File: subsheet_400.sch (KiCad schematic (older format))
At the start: 24 parts, among them U400 STE_GSTMCU_PHY

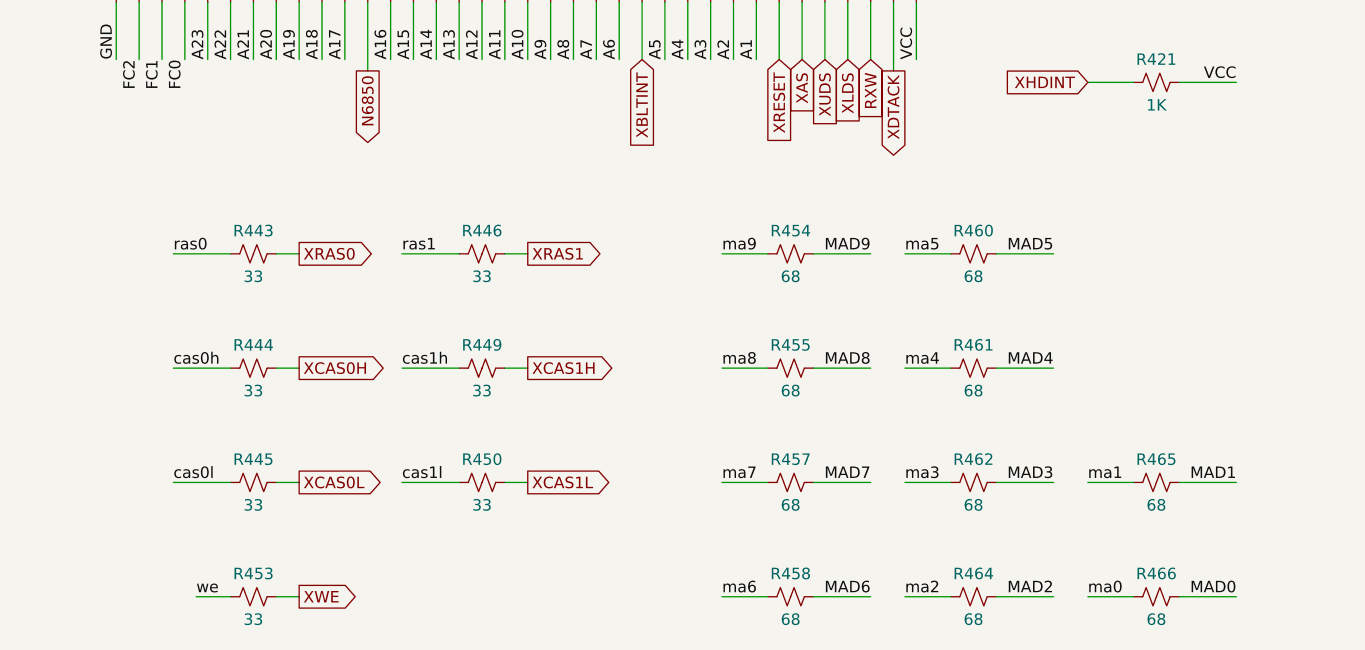
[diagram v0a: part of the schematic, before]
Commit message: Resolves #1 : Use 4-resistor packs wherever it is possible
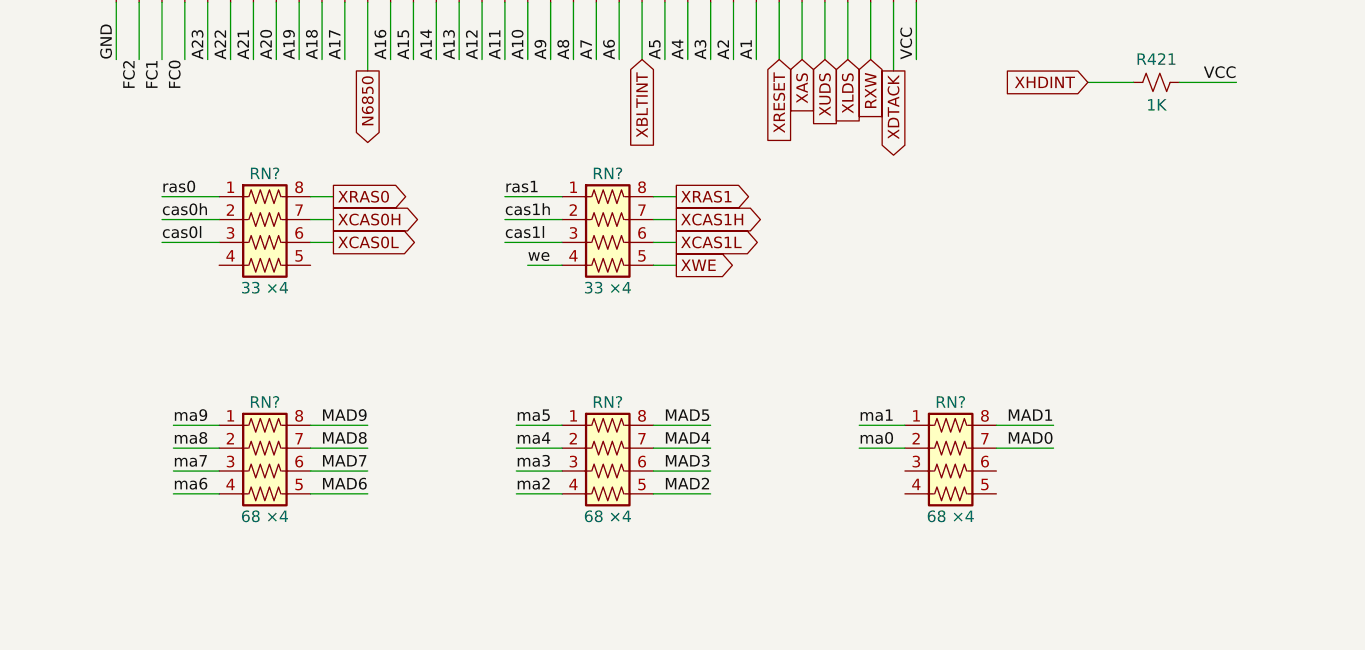
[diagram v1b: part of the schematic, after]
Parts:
- removed R443, R444, R445, R446, R449, R450, R453: 33, commons_passives_THT:Passive_THT_resistor_W2.54mm_L12.70mm, symbol Device:R_Small_US
- removed R454, R455, R457, R458, R460, R461, R462, R464, R465, R466: 68, commons_passives_THT:Passive_THT_resistor_W2.54mm_L12.70mm, symbol Device:R_Small_US
- added RN? (x2): 33 ×4, symbol custom_passives:R_Pack04_US
- added RN? (x3): 68 ×4, symbol custom_passives:R_Pack04_US
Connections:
- net MAD0: now also RN?.7 (R2.2)
- net MAD1: now also RN?.8 (R1.2)
- net MAD2: now also RN?.5 (R4.2)
- net MAD3: now also RN?.6 (R3.2)
- net MAD4: now also RN?.7 (R2.2)
- net MAD5: now also RN?.8 (R1.2)
- net MAD6: now also RN?.5 (R4.2)
- net MAD7: now also RN?.6 (R3.2)
- net MAD8: now also RN?.7 (R2.2)
- net MAD9: now also RN?.8 (R1.2)
- net XCAS0H: now also RN?.7 (R2.2)
- net XCAS0L: now also RN?.6 (R3.2)
- net XCAS1H: now also RN?.7 (R2.2)
- net XCAS1L: now also RN?.6 (R3.2)
- net XRAS0: now also RN?.8 (R1.2)
- net XRAS1: now also RN?.8 (R1.2)
- net XWE: now also RN?.5 (R4.2)
- net cas0h: now also RN?.2 (R2.1)
- net cas0l: now also RN?.3 (R3.1)
- net cas1h: now also RN?.2 (R2.1)
- net cas1l: now also RN?.3 (R3.1)
- net ma0: now also RN?.2 (R2.1)
- net ma1: now also RN?.1 (R1.1)
- net ma2: now also RN?.4 (R4.1)
- net ma3: now also RN?.3 (R3.1)
- net ma4: now also RN?.2 (R2.1)
- net ma5: now also RN?.1 (R1.1)
- net ma6: now also RN?.4 (R4.1)
- net ma7: now also RN?.3 (R3.1)
- net ma8: now also RN?.2 (R2.1)
- net ma9: now also RN?.1 (R1.1)
- net ras0: now also RN?.1 (R1.1)
- net ras1: now also RN?.1 (R1.1)
- net we: now also RN?.4 (R4.1)

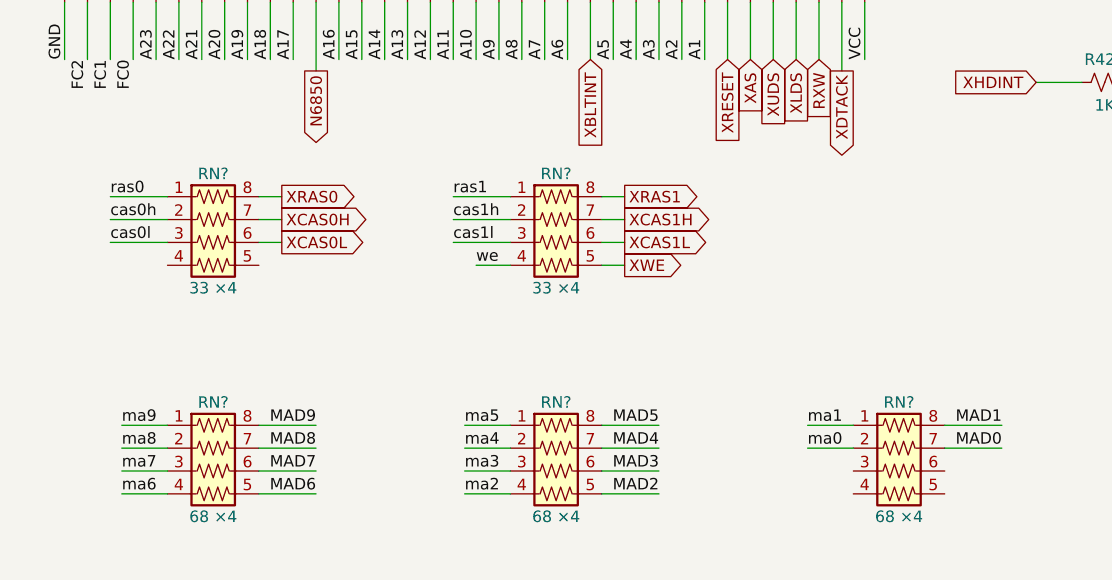
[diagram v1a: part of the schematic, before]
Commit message: annotate resistor networks and mark unused pins as unconnected
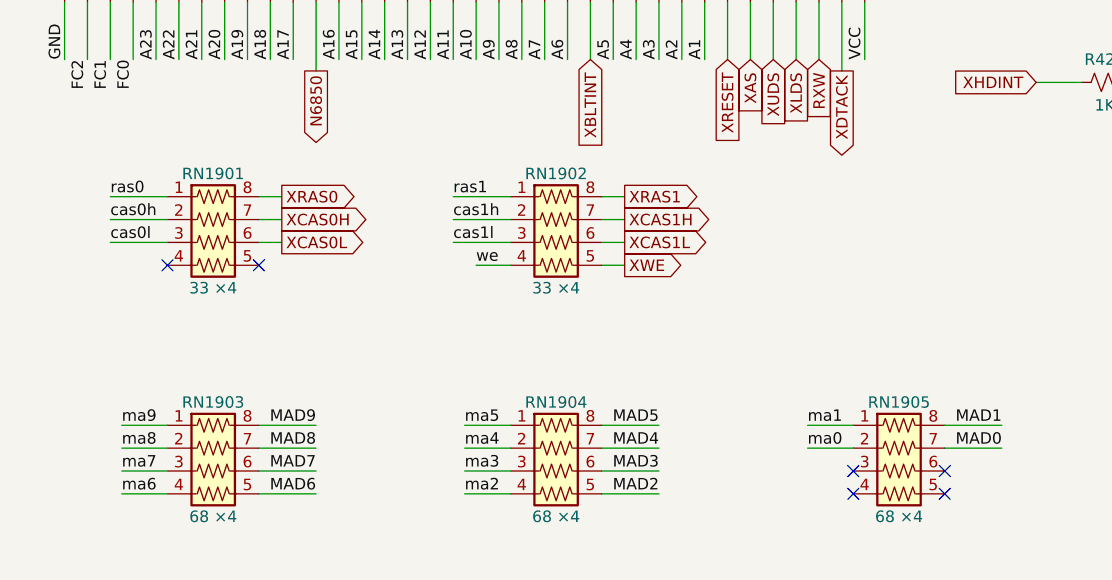
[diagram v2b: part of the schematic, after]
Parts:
- gave numbers to parts that had none: 5
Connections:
- no-connect marks 12 -> 18
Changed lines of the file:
@@
 	3550 7400 3550 7150
 $Comp
-L custom_passives:R_Pack04_US RN?
+L custom_passives:R_Pack04_US RN1901
 U 1 1 6229461F
 P 3000 8200
-F 0 "RN?" V 2700 8200 50  0000 C CNN
+F 0 "RN1901" V 2700 8200 50  0000 C CNN
 F 1 "33 ×4" V 3200 8200 50  0000 C CNN
 F 2 "" V 3275 8200 50  0001 C CNN
@@
 $EndComp
 $Comp
-L custom_passives:R_Pack04_US RN?
+L custom_passives:R_Pack04_US RN1902
 U 1 1 622CCFB9
 P 4500 8200
-F 0 "RN?" V 4200 8200 50  0000 C CNN
+F 0 "RN1902" V 4200 8200 50  0000 C CNN
 F 1 "33 ×4" V 4700 8200 50  0000 C CNN
 F 2 "" V 4775 8200 50  0001 C CNN
@@
 $EndComp
 $Comp
-L custom_passives:R_Pack04_US RN?
+L custom_passives:R_Pack04_US RN1903
 U 1 1 6233CA32
 P 3000 9200
-F 0 "RN?" V 2700 9200 50  0000 C CNN
+F 0 "RN1903" V 2700 9200 50  0000 C CNN
 F 1 "68 ×4" V 3200 9200 50  0000 C CNN
 F 2 "" V 3275 9200 50  0001 C CNN
@@
 $EndComp
 $Comp
-L custom_passives:R_Pack04_US RN?
+L custom_passives:R_Pack04_US RN1904
 U 1 1 623874D8
 P 4500 9200
-F 0 "RN?" V 4200 9200 50  0000 C CNN
+F 0 "RN1904" V 4200 9200 50  0000 C CNN
 F 1 "68 ×4" V 4700 9200 50  0000 C CNN
 F 2 "" V 4775 9200 50  0001 C CNN
@@
 $EndComp
 $Comp
-L custom_passives:R_Pack04_US RN?
+L custom_passives:R_Pack04_US RN1905
 U 1 1 623D2AD5
 P 6000 9200
-F 0 "RN?" V 5700 9200 50  0000 C CNN
+F 0 "RN1905" V 5700 9200 50  0000 C CNN
 F 1 "68 ×4" V 6200 9200 50  0000 C CNN
 F 2 "" V 6275 9200 50  0001 C CNN
@@
 	0    1    1    0
 $EndComp
+NoConn ~ 2800 8300
+NoConn ~ 3200 8300
+NoConn ~ 5800 9200
+NoConn ~ 6200 9200
+NoConn ~ 5800 9300
+NoConn ~ 6200 9300
 $EndSCHEMATC

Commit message: Resolves #7 : Assign SMD footprints to resistors pack
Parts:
- RN1901, RN1902, RN1903, RN1904, RN1905: footprint (none) -> Resistor_SMD:R_Array_Convex_4x0603
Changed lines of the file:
@@
 F 0 "RN1901" V 2700 8200 50  0000 C CNN
 F 1 "33 ×4" V 3200 8200 50  0000 C CNN
-F 2 "" V 3275 8200 50  0001 C CNN
+F 2 "Resistor_SMD:R_Array_Convex_4x0603" V 3275 8200 50  0001 C CNN
 F 3 "~" H 3000 8200 50  0001 C CNN
 	1    3000 8200
@@
 F 0 "RN1902" V 4200 8200 50  0000 C CNN
 F 1 "33 ×4" V 4700 8200 50  0000 C CNN
-F 2 "" V 4775 8200 50  0001 C CNN
+F 2 "Resistor_SMD:R_Array_Convex_4x0603" V 4775 8200 50  0001 C CNN
 F 3 "~" H 4500 8200 50  0001 C CNN
 	1    4500 8200
@@
 F 0 "RN1903" V 2700 9200 50  0000 C CNN
 F 1 "68 ×4" V 3200 9200 50  0000 C CNN
-F 2 "" V 3275 9200 50  0001 C CNN
+F 2 "Resistor_SMD:R_Array_Convex_4x0603" V 3275 9200 50  0001 C CNN
 F 3 "~" H 3000 9200 50  0001 C CNN
 	1    3000 9200
@@
 F 0 "RN1904" V 4200 9200 50  0000 C CNN
 F 1 "68 ×4" V 4700 9200 50  0000 C CNN
-F 2 "" V 4775 9200 50  0001 C CNN
+F 2 "Resistor_SMD:R_Array_Convex_4x0603" V 4775 9200 50  0001 C CNN
 F 3 "~" H 4500 9200 50  0001 C CNN
 	1    4500 9200
@@
 F 0 "RN1905" V 5700 9200 50  0000 C CNN
 F 1 "68 ×4" V 6200 9200 50  0000 C CNN
-F 2 "" V 6275 9200 50  0001 C CNN
+F 2 "Resistor_SMD:R_Array_Convex_4x0603" V 6275 9200 50  0001 C CNN
 F 3 "~" H 6000 9200 50  0001 C CNN
 	1    6000 9200

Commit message: Resolves #13 : assign 1206 hand-solder footprints to resistors
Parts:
- R421: footprint commons_passives_THT:Passive_THT_resistor_W2.54mm_L12.70mm -> Resistor_SMD:R_1206_3216Metric_Pad1.30x1.75mm_HandSolder
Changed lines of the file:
@@
 F 0 "R421" V 6800 7500 50  0000 C CNN
 F 1 "1K" V 7000 7500 50  0000 C CNN
-F 2 "commons_passives_THT:Passive_THT_resistor_W2.54mm_L12.70mm" H 6900 7500 50  0001 C CNN
+F 2 "Resistor_SMD:R_1206_3216Metric_Pad1.30x1.75mm_HandSolder" H 6900 7500 50  0001 C CNN
 F 3 "~" H 6900 7500 50  0001 C CNN
 	1    6900 7500

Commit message: Resolves #8 : Assign 1206 hand-solder footprints to non polarized capacitors
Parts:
- C402, C403, C404, C405, C406: footprint commons_passives_THT:Passive_THT_capacitor_mlcc_W2.54mm_L7.62mm -> Capacitor_SMD:C_1206_3216Metric_Pad1.33x1.80mm_HandSolder
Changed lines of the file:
@@
 F 0 "C402" H 1125 7350 50  0000 L CNN
 F 1 "0.1uF" H 1125 7150 50  0000 L CNN
-F 2 "commons_passives_THT:Passive_THT_capacitor_mlcc_W2.54mm_L7.62mm" H 1138 7100 50  0001 C CNN
+F 2 "Capacitor_SMD:C_1206_3216Metric_Pad1.33x1.80mm_HandSolder" H 1138 7100 50  0001 C CNN
 F 3 "~" H 1100 7250 50  0001 C CNN
 	1    1100 7250
@@
 F 0 "C403" H 1625 7350 50  0000 L CNN
 F 1 "0.1uF" H 1625 7150 50  0000 L CNN
-F 2 "commons_passives_THT:Passive_THT_capacitor_mlcc_W2.54mm_L7.62mm" H 1638 7100 50  0001 C CNN
+F 2 "Capacitor_SMD:C_1206_3216Metric_Pad1.33x1.80mm_HandSolder" H 1638 7100 50  0001 C CNN
 F 3 "~" H 1600 7250 50  0001 C CNN
 	1    1600 7250
@@
 F 0 "C404" H 1125 8350 50  0000 L CNN
 F 1 "0.1uF" H 1125 8150 50  0000 L CNN
-F 2 "commons_passives_THT:Passive_THT_capacitor_mlcc_W2.54mm_L7.62mm" H 1138 8100 50  0001 C CNN
+F 2 "Capacitor_SMD:C_1206_3216Metric_Pad1.33x1.80mm_HandSolder" H 1138 8100 50  0001 C CNN
 F 3 "~" H 1100 8250 50  0001 C CNN
 	1    1100 8250
@@
 F 0 "C405" H 1625 8350 50  0000 L CNN
 F 1 "0.1uF" H 1625 8150 50  0000 L CNN
-F 2 "commons_passives_THT:Passive_THT_capacitor_mlcc_W2.54mm_L7.62mm" H 1638 8100 50  0001 C CNN
+F 2 "Capacitor_SMD:C_1206_3216Metric_Pad1.33x1.80mm_HandSolder" H 1638 8100 50  0001 C CNN
 F 3 "~" H 1600 8250 50  0001 C CNN
 	1    1600 8250
@@
 F 0 "C406" H 1125 9350 50  0000 L CNN
 F 1 "0.1uF" H 1125 9150 50  0000 L CNN
-F 2 "commons_passives_THT:Passive_THT_capacitor_mlcc_W2.54mm_L7.62mm" H 1138 9100 50  0001 C CNN
+F 2 "Capacitor_SMD:C_1206_3216Metric_Pad1.33x1.80mm_HandSolder" H 1138 9100 50  0001 C CNN
 F 3 "~" H 1100 9250 50  0001 C CNN
 	1    1100 9250
